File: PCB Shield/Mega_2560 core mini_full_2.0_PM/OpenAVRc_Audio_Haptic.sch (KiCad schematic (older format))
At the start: 14 parts, among them P22 JQ6500_28P, P27 HP, P5 Vibreur, P8 Audio

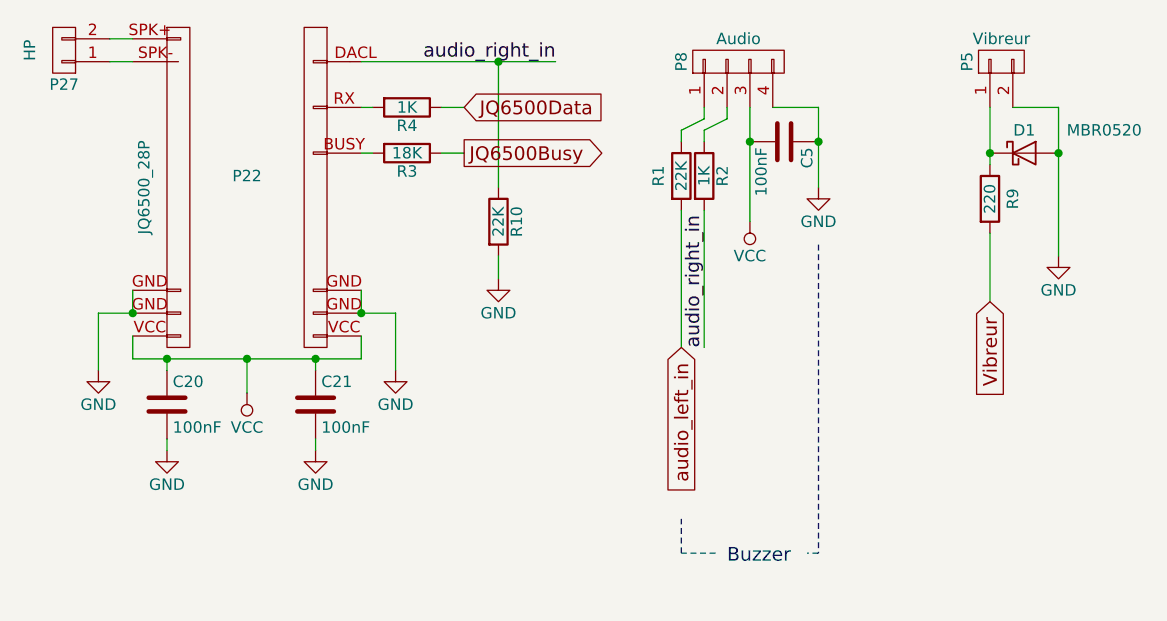
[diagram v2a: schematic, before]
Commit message: Some changes on schematic's shield (JQ and haptic labels)
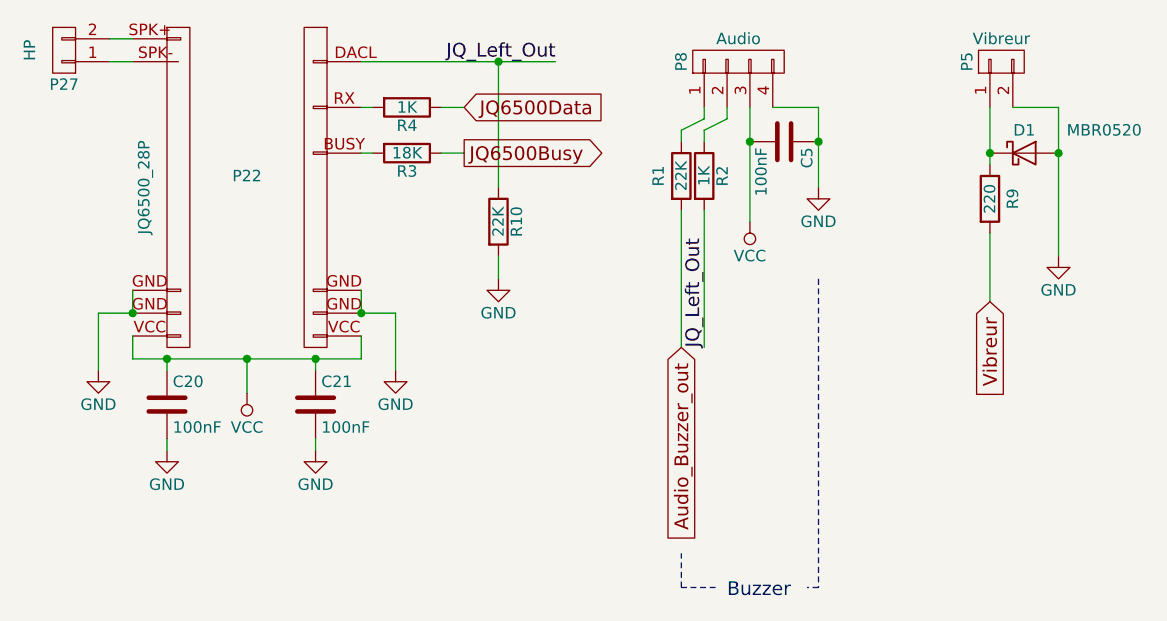
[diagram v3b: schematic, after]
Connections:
- net audio_left_in renamed Audio_Buzzer_out
- net audio_right_in renamed JQ_Left_Out
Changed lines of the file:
@@
 $EndComp
 Text Label 6000 4300 1    60   ~ 0
-audio_right_in
+JQ_Left_Out
 $Comp
 L C-RESCUE-Mega_2560_core_mini_full_2.0 C5
@@
 $EndComp
 Text Label 5350 3050 2    60   ~ 0
-audio_right_in
+JQ_Left_Out
 $Comp
 L R-RESCUE-Mega_2560_core_mini_full_2.0 R3
@@
 	0    -1   -1   0
 $EndComp
-Text Notes 6100 5250 0    60   ~ 0
+Text Notes 6100 5400 0    60   ~ 0
 Buzzer
 $Comp
@@
 	6000 3300 6000 3250
 Wire Notes Line
-	6500 3850 6500 5200
+	6500 4000 6500 5350
 Wire Notes Line
-	6500 5200 6450 5200
+	6500 5350 6450 5350
 Wire Notes Line
-	6050 5200 5900 5200
+	6050 5350 5900 5350
 Wire Notes Line
-	5900 5200 5900 5050
+	5900 5350 5900 5200
 Wire Wire Line
 	5100 3600 5100 3050
@@
 	3650 4700 3650 4750
 Text GLabel 5900 4300 3    60   Input ~ 0
-audio_left_in
+Audio_Buzzer_out
 Text GLabel 4950 3250 2    60   Input ~ 0
 JQ6500Data

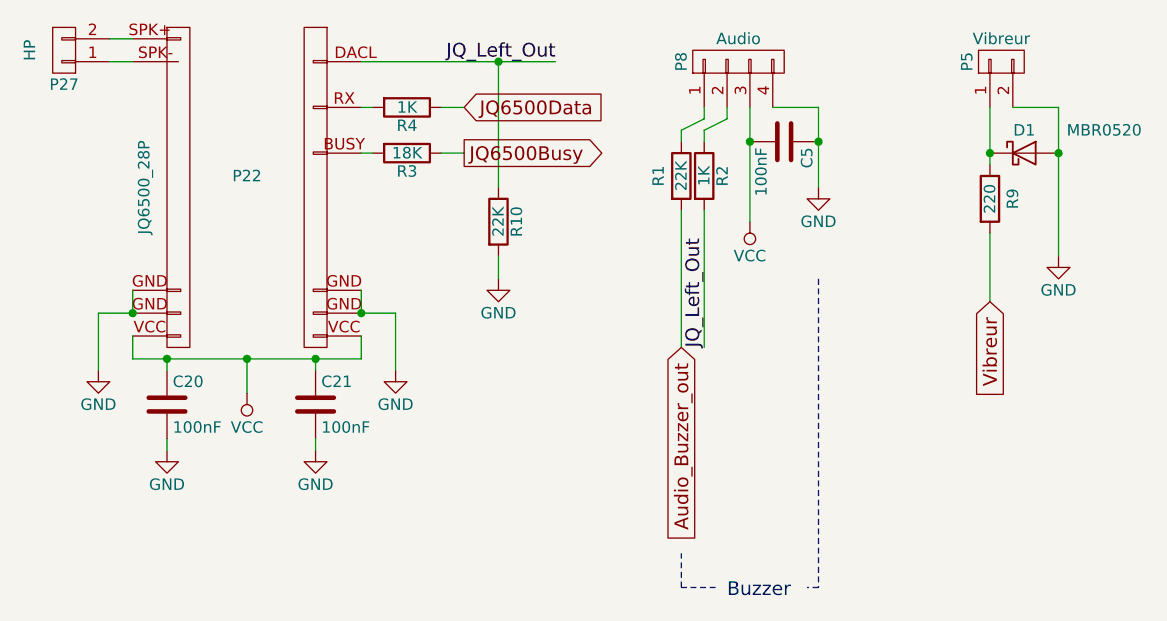
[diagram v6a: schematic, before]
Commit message: Re-update_shield_schéma
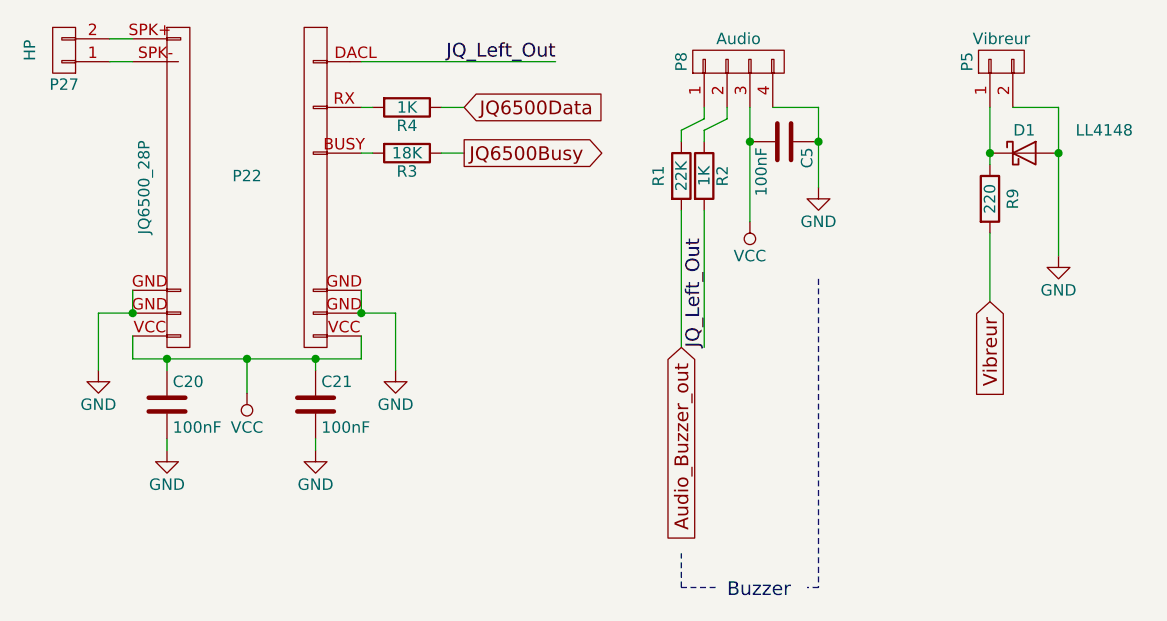
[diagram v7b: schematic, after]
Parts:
- removed R10: 22K, Resistors_SMD:R_1206, symbol R-RESCUE-Mega_2560_core_mini_full_2.0
- D1: value MBR0520 -> LL4148
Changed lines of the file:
@@
 Sheet 6 7
 Title "Shield Mega2560 core Full"
-Date "2017-11-12"
+Date "2018-01-27"
 Rev "2.00"
 Comp "© Team OpenAVRc"
@@
 P 7400 3450
 F 0 "D1" H 7400 3550 50  0000 C CNN
-F 1 "MBR0520" H 7750 3550 50  0000 C CNN
+F 1 "LL4148" H 7750 3550 50  0000 C CNN
 F 2 "Diodes_SMD:D_SOD-123" H 7400 3275 50  0001 C CNN
 F 3 "" H 7400 3450 50  0001 C CNN
@@
 Buzzer
 $Comp
-L R-RESCUE-Mega_2560_core_mini_full_2.0 R10
-U 1 1 59C5A5C4
-P 5100 3750
-F 0 "R10" V 5180 3750 50  0000 C CNN
-F 1 "22K" V 5100 3750 50  0000 C CNN
-F 2 "Resistors_SMD:R_1206" V 5030 3750 50  0001 C CNN
-F 3 "" H 5100 3750 50  0000 C CNN
-	1    5100 3750
-	1    0    0    -1
-$EndComp
-$Comp
-L GND-RESCUE-Mega_2560_core_mini_full_2.0 #PWR0110
-U 1 1 59C5A5CB
-P 5100 4000
-F 0 "#PWR0110" H 5100 3750 50  0001 C CNN
-F 1 "GND" H 5100 3850 50  0000 C CNN
-F 2 "" H 5100 4000 50  0000 C CNN
-F 3 "" H 5100 4000 50  0000 C CNN
-	1    5100 4000
-	1    0    0    -1
-$EndComp
-$Comp
 L C-RESCUE-Mega_2560_core_mini_full_2.0 C20
 U 1 1 59C5A5D1
@@
 	5900 5350 5900 5200
 Wire Wire Line
-	5100 3600 5100 3050
-Connection ~ 5100 3050
-Wire Wire Line
-	5100 3900 5100 4000
-Wire Wire Line
 	3650 4400 3650 4350
